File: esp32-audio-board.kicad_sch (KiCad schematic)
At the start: 120 parts, among them IC1 XC6220A331MR-G, IC2 XC6220A331MR-G, J1 EN_PAD0, J10 PWR_LED+, J11 HP_LOUT1, J12 HP_ROUT1, J13 HP_LOUT2, J14 HP_ROUT2, J15 MIC_LIN1, J16 MIC_LIN1_GND, J17 MIC_RIN1, J18 MIC_RIN1_GND, J19 HP_1GND, J2 Conn_01x02_Pin, J20 HP_2GND, J21 VP_PAD0, J22 PWR_LED-, J23 CHG_LED+, J24 CHG_LED-, J3 USB_C_Receptacle_USB2.0_16P, J4 EN_PAD1, J5 VP_PAD1, J6 VN_PAD0, J7 VN_PAD1, J8 IO14_PAD0, J9 IO14_PAD1, Q1 SS8050, Q2 SS8050, Q4 AO3401A, U1 ESP32-WROOM-32E, U2 CH340C, U3 MCP73831-2-OT, U5 ES8388

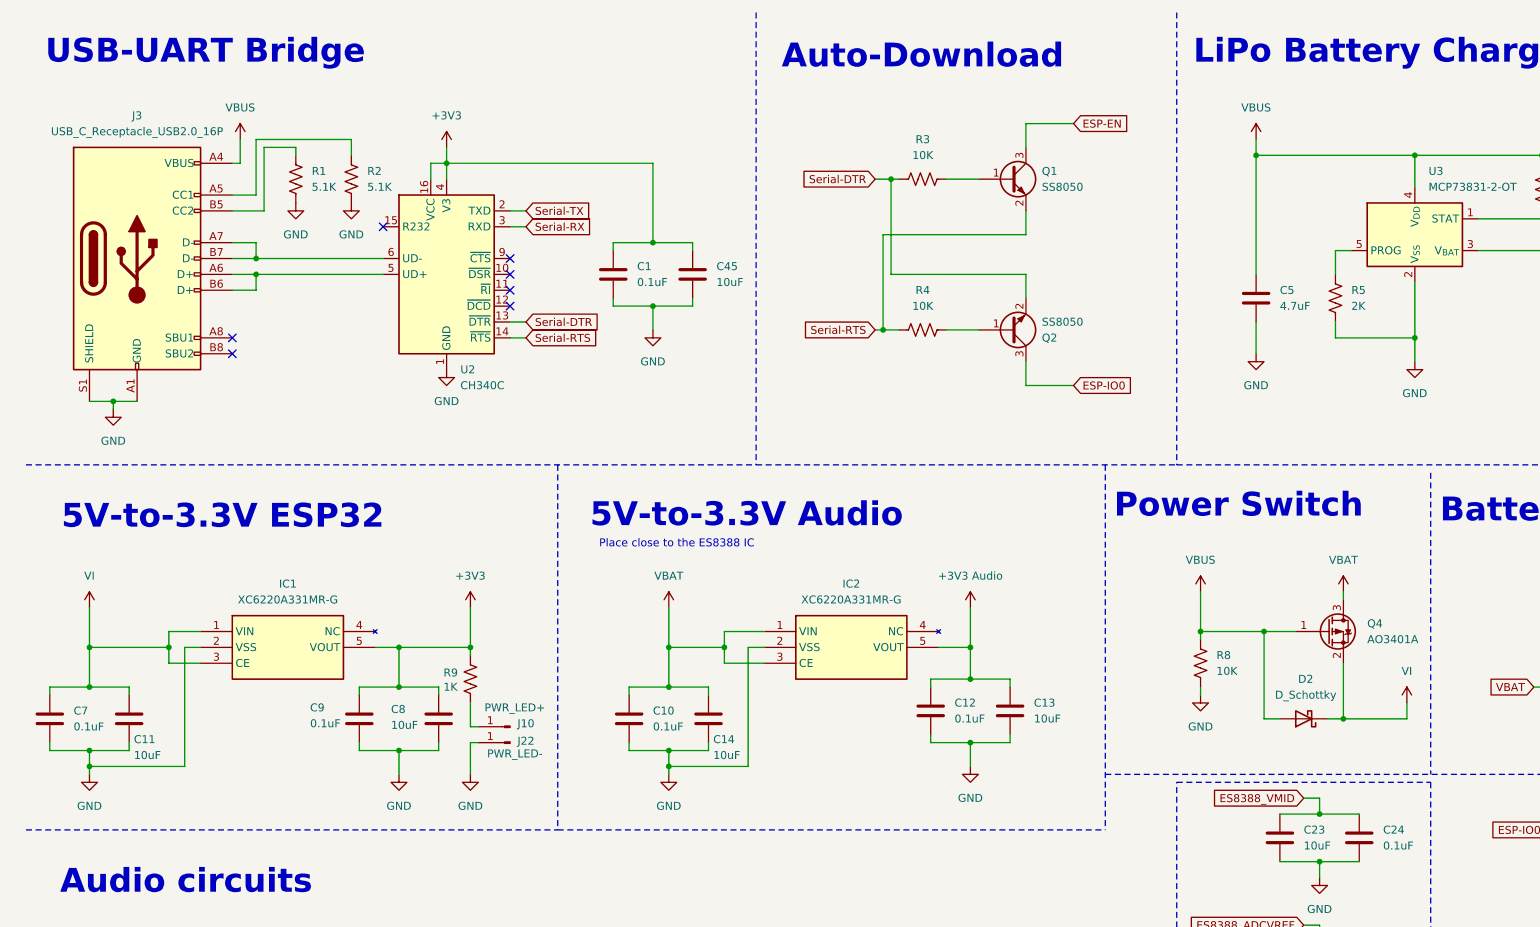
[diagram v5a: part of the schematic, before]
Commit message: esp32-audio-board: add ferrite beads on pwr lanes
Added two ferrite beads (BLM) on the high power
rails - from USB-C/battery, to lower the EMI.

Added some little improvements to the schematic and PCB.

Signed-off-by: RaresCon <rares.constantin2002@gmail.com>
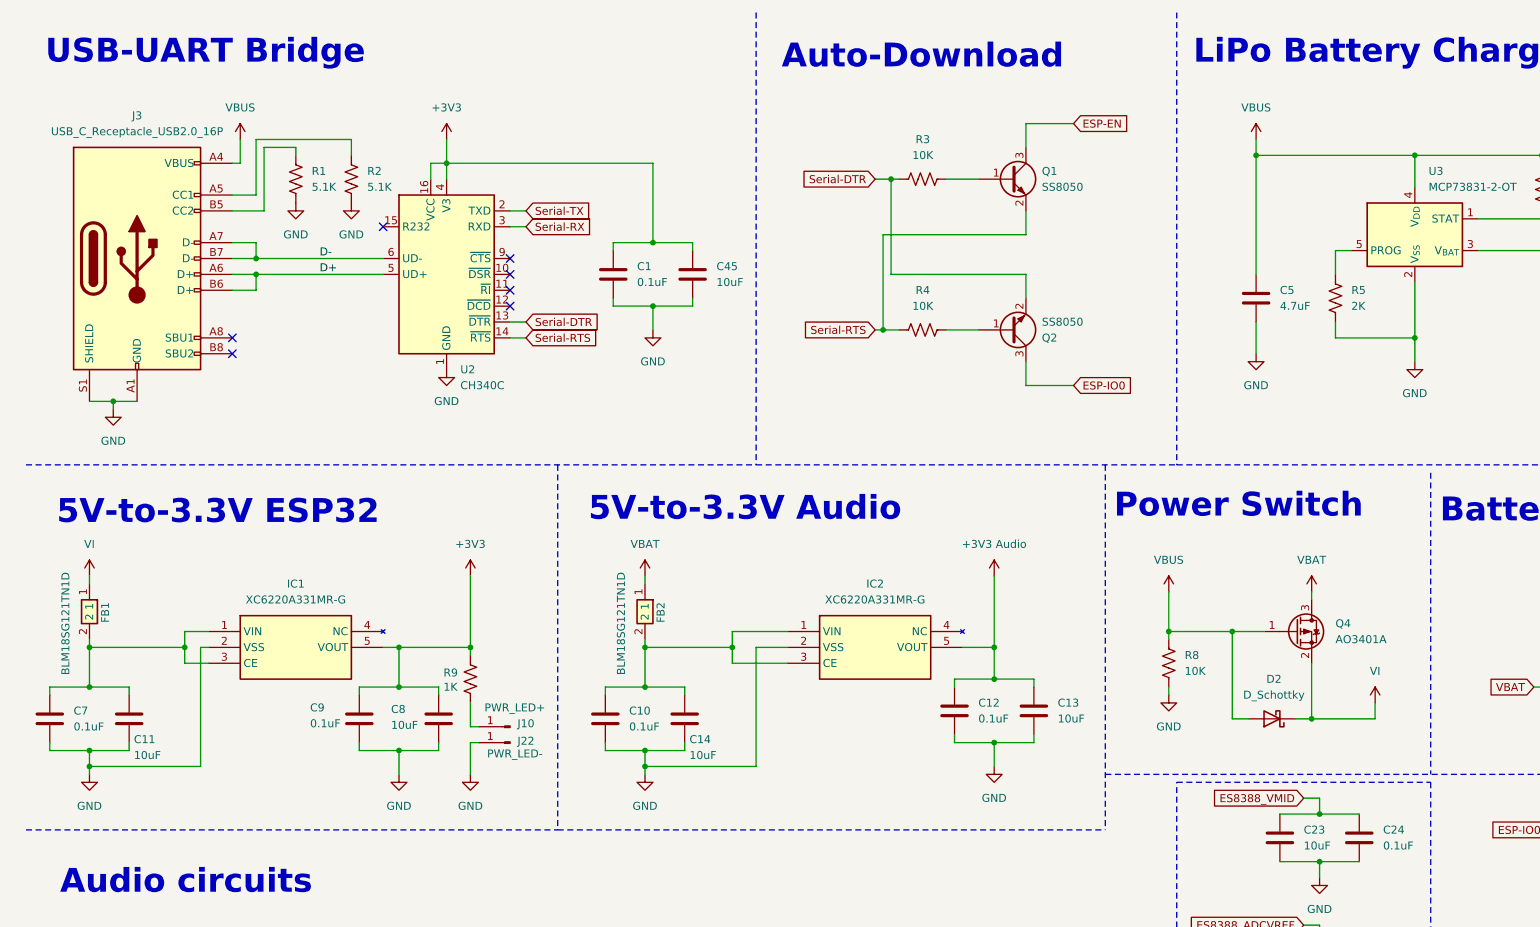
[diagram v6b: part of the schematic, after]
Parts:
- added FB1, FB2: BLM18SG121TN1D, BLM18EG101TH1D, symbol BLM18SG121TN1D:BLM18SG121TN1D
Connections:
- net VBAT: now also FB2.1; no longer C10.1, C14.1, IC2.1 (VIN), IC2.3 (CE)
- net VI: now also FB1.1; no longer C11.1, C7.1, IC1.1 (VIN), IC1.3 (CE)
- net D+: now reaches J3.A6 (D+), J3.B6 (D+), U2.5 (UD+)
- net D-: now reaches J3.A7 (D-), J3.B7 (D-), U2.6 (UD-)
- new net: C10.1, C14.1, FB2.2, IC2.1 (VIN), IC2.3 (CE)
- new net: C11.1, C7.1, FB1.2, IC1.1 (VIN), IC1.3 (CE)
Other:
- note removed: "Place close to the ES8388 IC"
- moved on the sheet: C10, C12, C13, C14, D2, IC1, IC2, Q4, R8

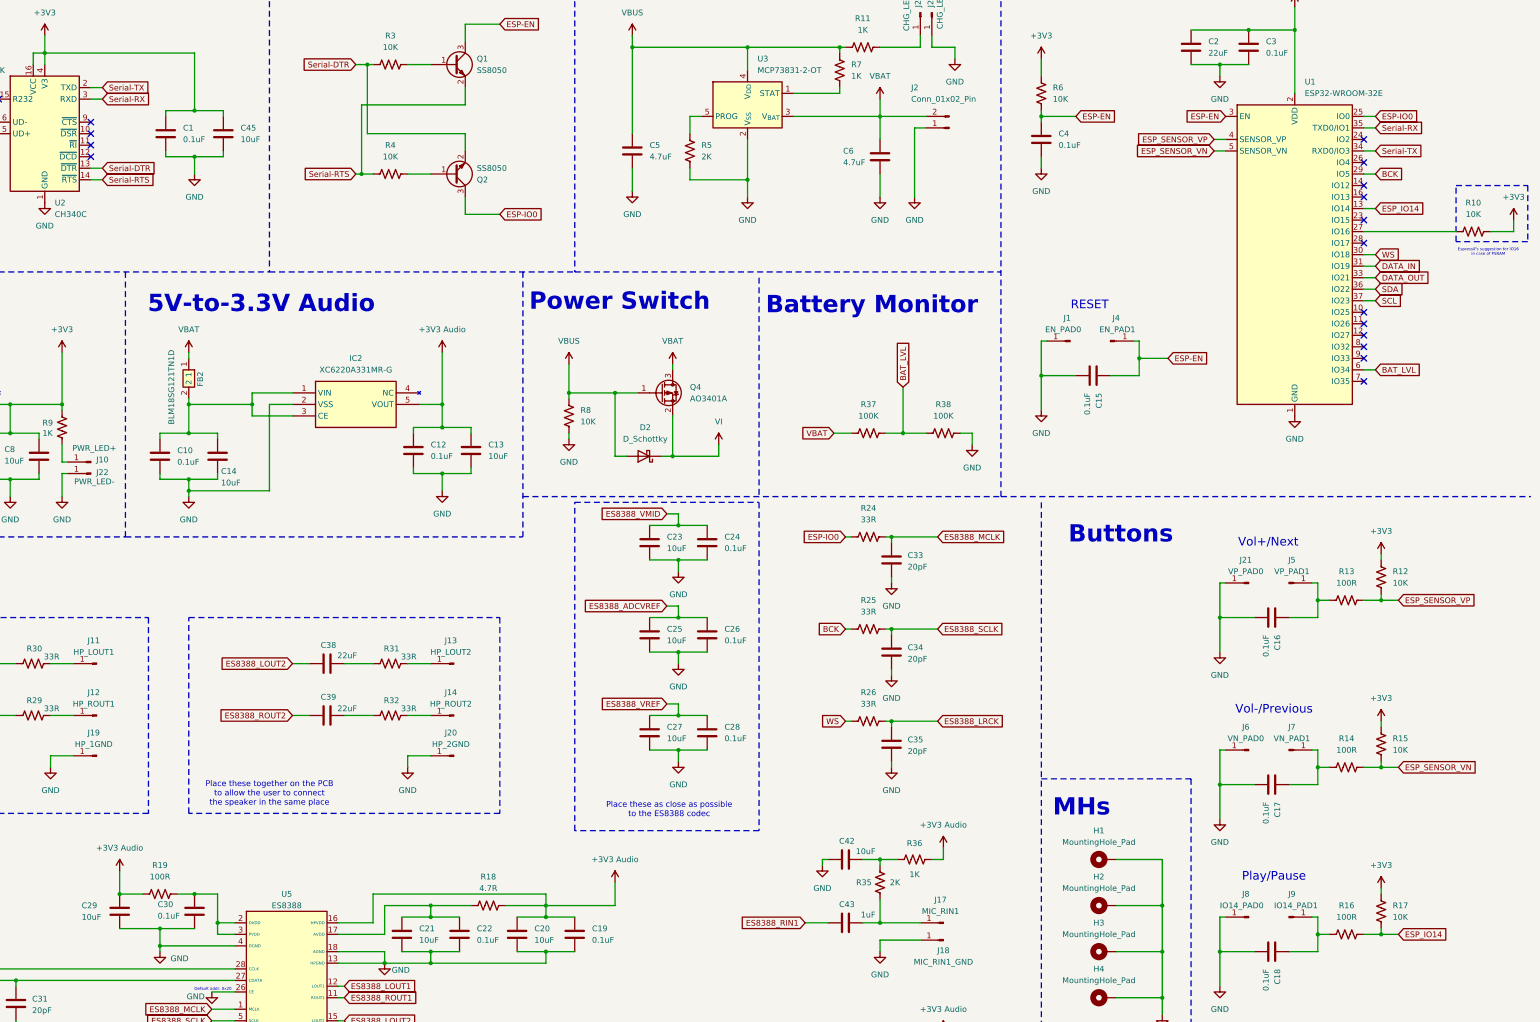
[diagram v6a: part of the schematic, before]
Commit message: esp32-audio-board: rehook ES8388
Rehooked the ES8388 to allow the routing to be
easier and allow ground planes under the I2C and
I2S to limit EMI and noise.

Signed-off-by: RaresCon <rares.constantin2002@gmail.com>
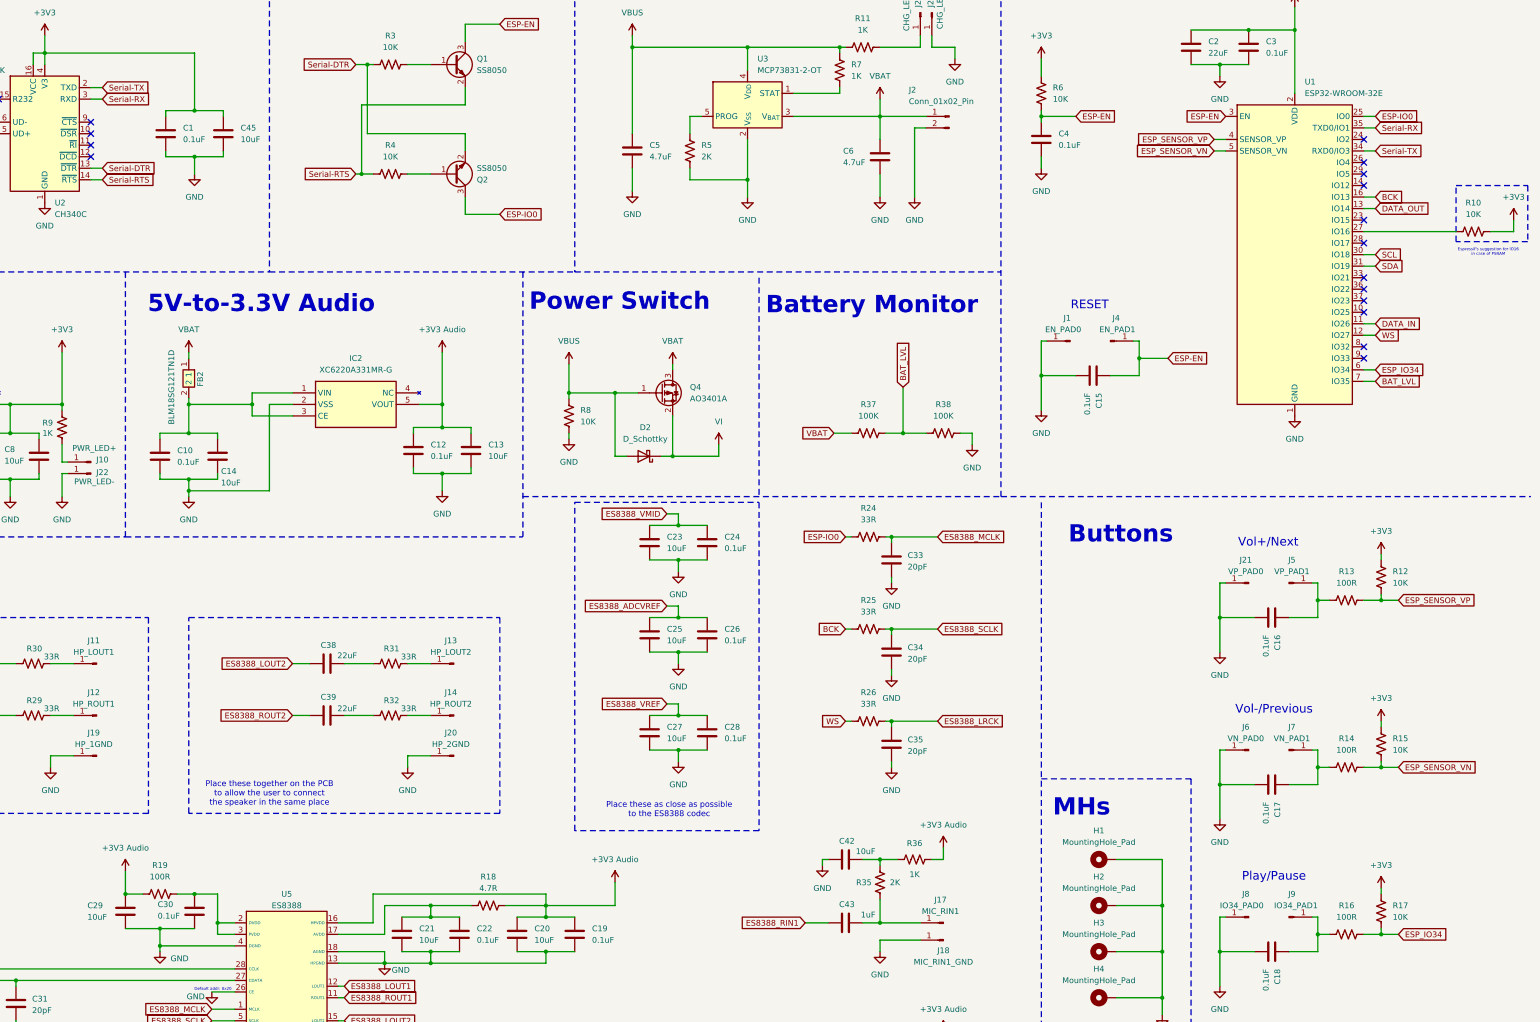
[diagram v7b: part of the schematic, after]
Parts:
- J8: value IO14_PAD0 -> IO34_PAD0
- J9: value IO14_PAD1 -> IO34_PAD1
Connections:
- net BAT_LVL: now also U1.7 (IO35); no longer U1.6 (IO34)
- net BCK: now also U1.16 (IO13); no longer U1.29 (IO5)
- net DATA_IN: now also U1.11 (IO26); no longer U1.31 (IO19)
- net DATA_OUT: now also U1.13 (IO14); no longer U1.33 (IO21)
- net GND: now also J2.2 (Pin_2); no longer J2.1 (Pin_1)
- net SCL: now also U1.30 (IO18); no longer U1.37 (IO23)
- net SDA: now also U1.31 (IO19); no longer U1.36 (IO22)
- net VBAT: now also J2.1 (Pin_1); no longer J2.2 (Pin_2)
- net WS: now also U1.12 (IO27); no longer U1.30 (IO18)
- net ESP_IO14 renamed ESP_IO34
- net ESP_IO34: now also U1.6 (IO34); no longer U1.13 (IO14)
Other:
- moved on the sheet: C29

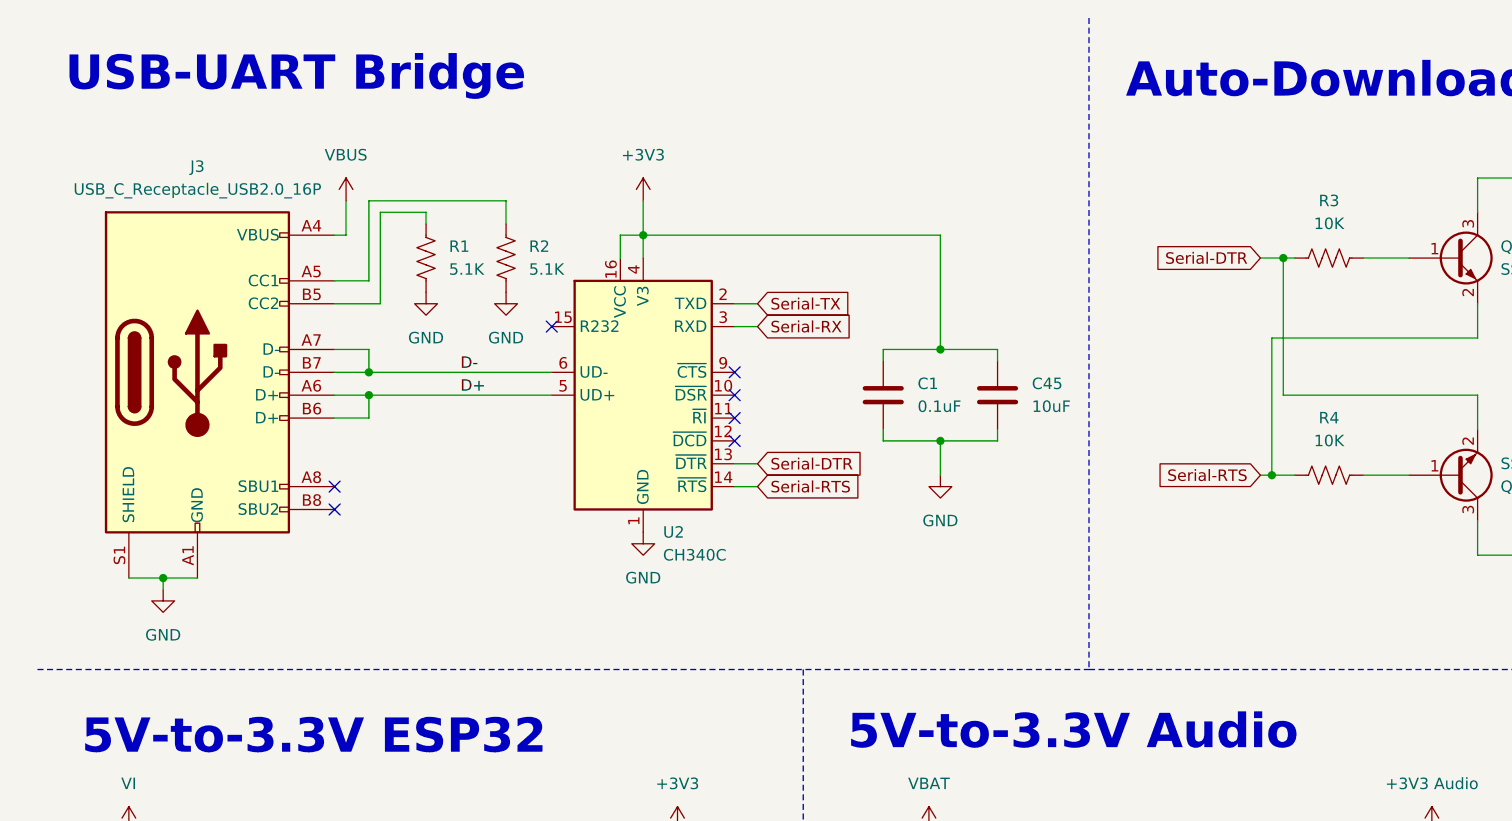
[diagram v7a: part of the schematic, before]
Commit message: esp32-audio-board: route initial power
Added routing for the USB-C and battery initial
lanes/traces to also see how small the PCB can
be as width.

Signed-off-by: RaresCon <rares.constantin2002@gmail.com>
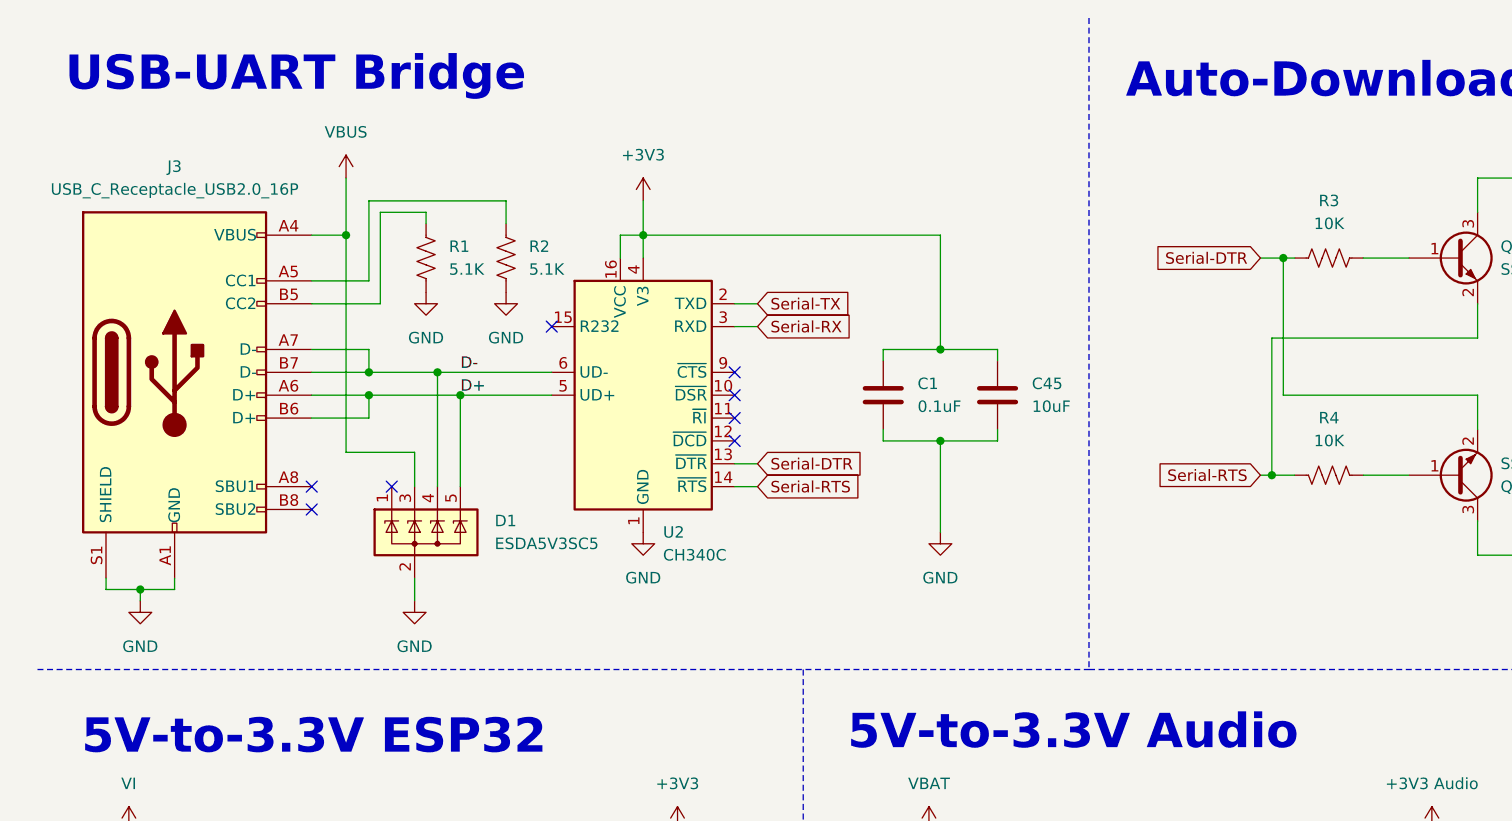
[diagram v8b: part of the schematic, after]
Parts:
- added D1: ESDA5V3SC5, Package_TO_SOT_SMD:SOT-23-5_HandSoldering, symbol Power_Protection:ESDA5V3SC5
- J3: footprint Connector_USB:USB_C_Receptacle_GCT_USB4110 -> Connector_USB:USB_C_Receptacle_GCT_USB4105-xx-A_16P_TopMnt_Horizontal
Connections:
- net D+: now also D1.5 (K)
- net D-: now also D1.4 (K)
- net GND: now also D1.2 (A)
- net Serial-RTS: now also R4.2; no longer R4.1
- net VBUS: now also D1.3 (K)
- net at Q2.1 (B): now also R4.1; no longer R4.2
- no-connect marks 21 -> 22
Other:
- moved on the sheet: J3, R4
